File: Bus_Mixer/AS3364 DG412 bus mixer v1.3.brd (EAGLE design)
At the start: 84.8 x 52.5 mm, 123 parts, among them IC1 PCA9539PW, IC10 DG412-J, IC11 DG412-J, IC2 TL074JT, IC3 TL072JT, IC4 TL074JT, IC5 TL072JT, IC6 TL072JT, IC8 DG412-J, IC9 DG412-J

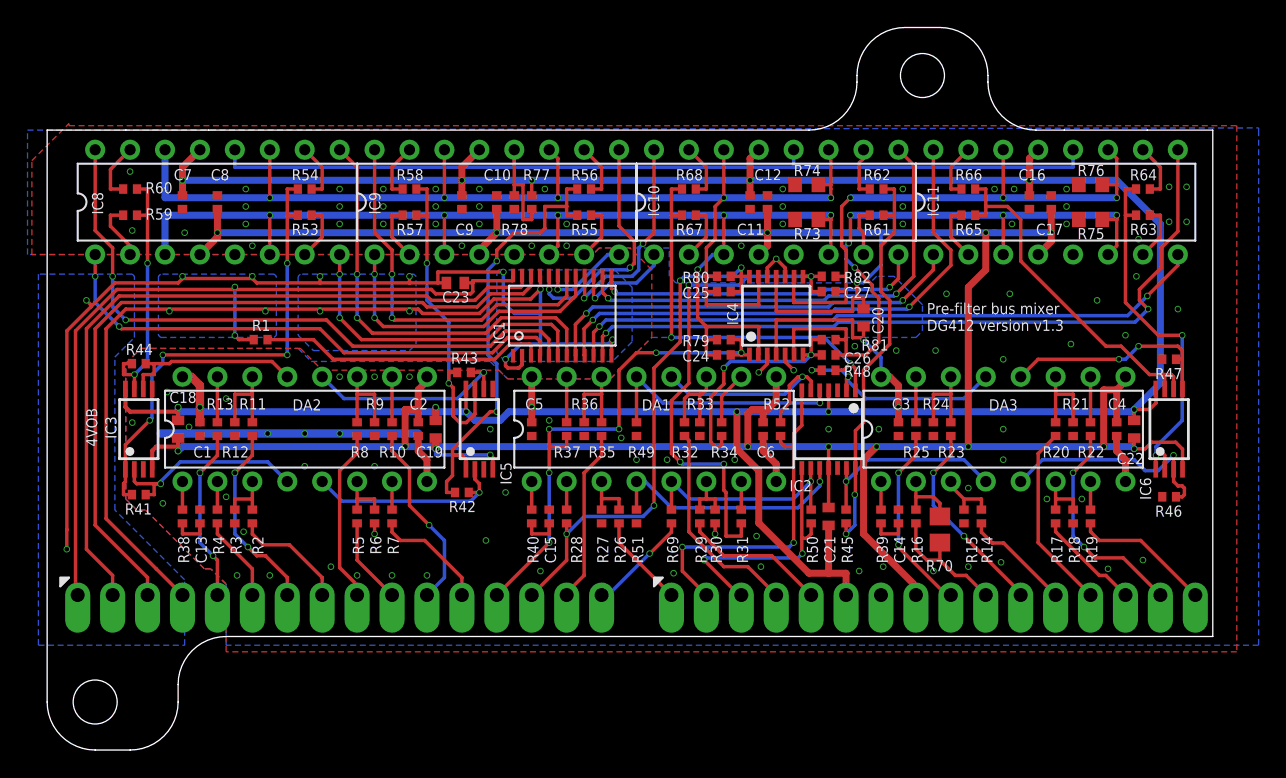
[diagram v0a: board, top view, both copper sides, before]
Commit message: Increased via outer diameter
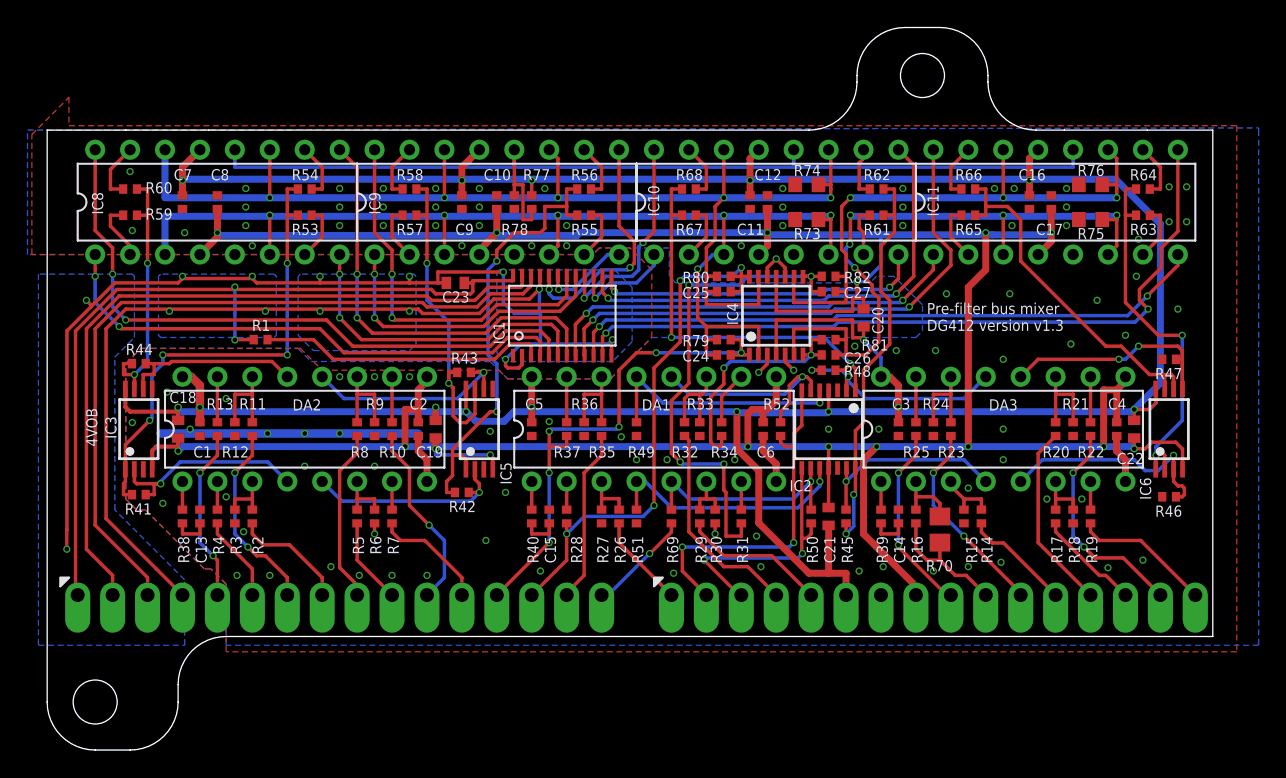
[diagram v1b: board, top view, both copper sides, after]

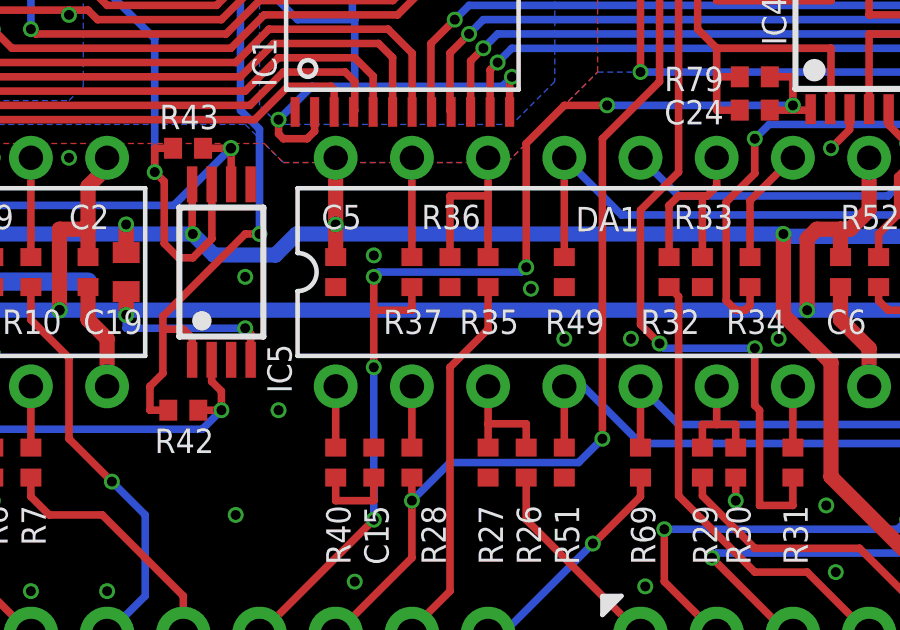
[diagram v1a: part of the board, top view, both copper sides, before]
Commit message: Fixed weird airwire
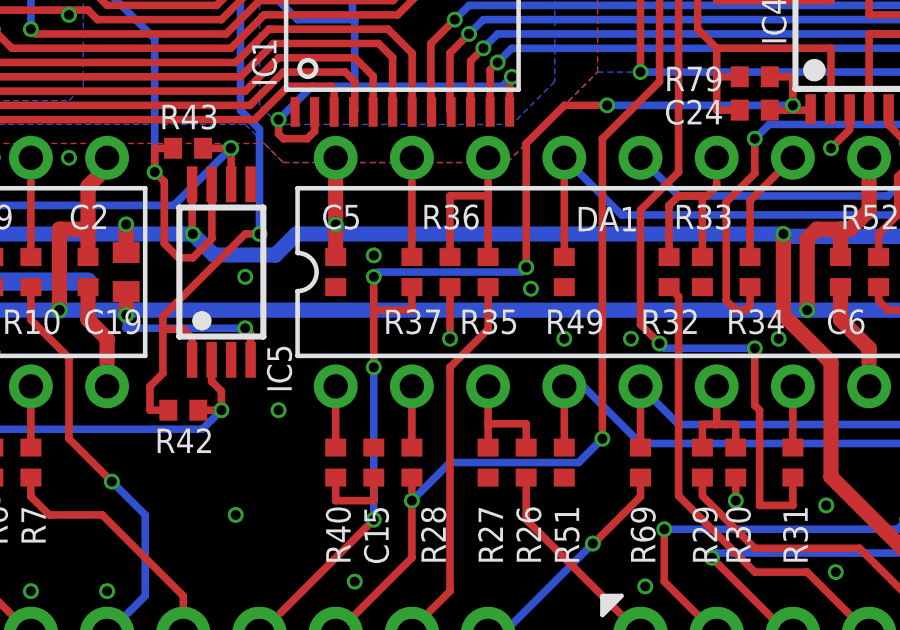
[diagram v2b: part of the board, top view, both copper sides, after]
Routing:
- net GND: track 37.2 -> 39.0 mm, vias 105 -> 106
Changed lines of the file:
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@@
 <via x="50.64125" y="7.3025" extent="1-16" drill="0.3302"/>
 <via x="76.2" y="5.000625" extent="1-16" drill="0.3302"/>
-<wire x1="40.79875" y1="14.525625" x2="38.1" y2="14.58125" width="0" layer="19" extent="1-1"/>
+<wire x1="38.1" y1="14.58125" x2="38.1" y2="12.85875" width="0.254" layer="1"/>
+<via x="38.1" y="12.85875" extent="1-16" drill="0.3302"/>
 </signal>
 <signal name="IN3">
